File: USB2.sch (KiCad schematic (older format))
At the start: 26 parts

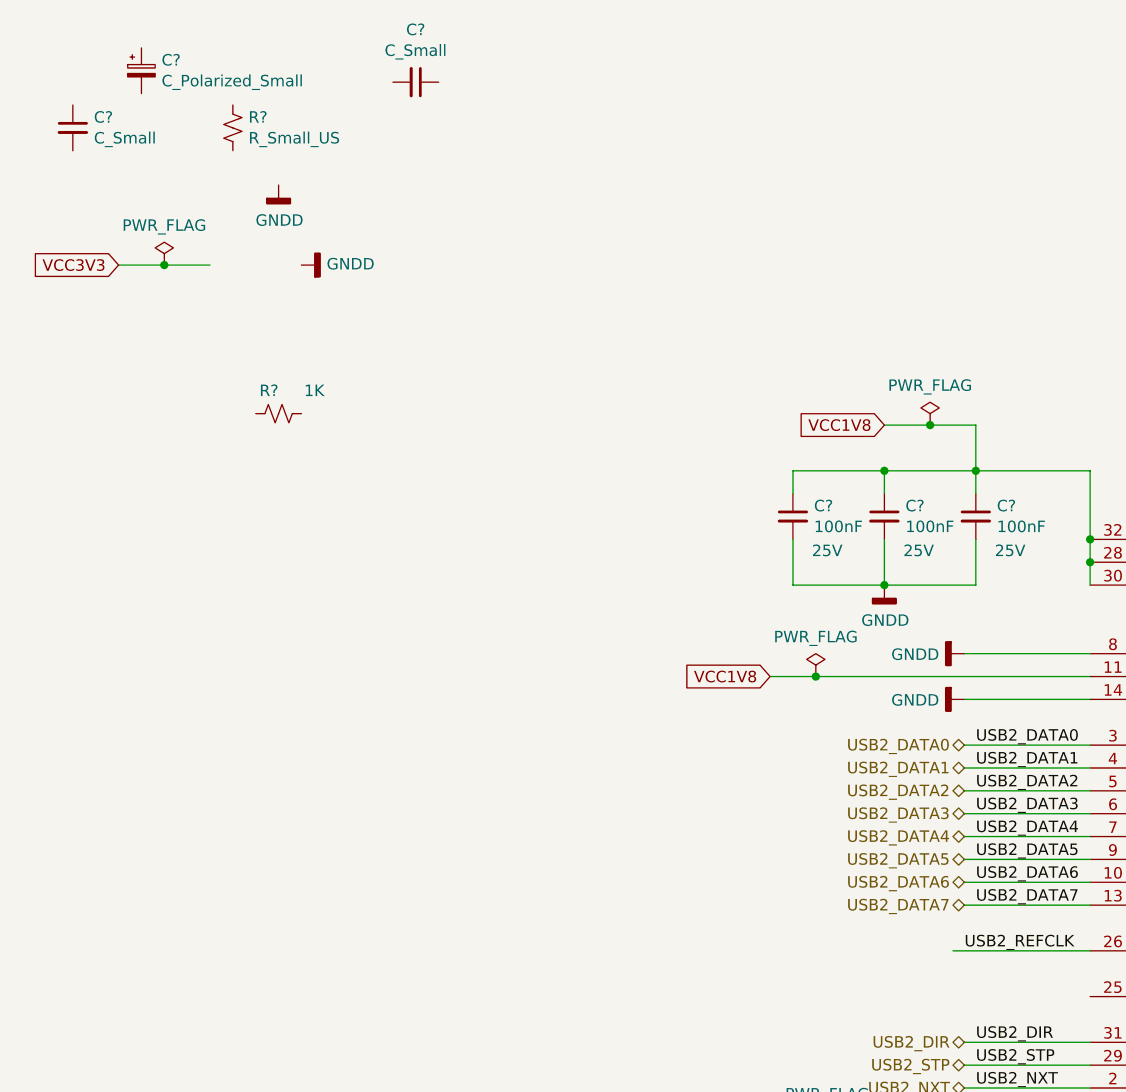
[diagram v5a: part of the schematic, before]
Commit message: Added bus lines -ETH_PHY_CONN -RAM -USB2 Made Output the port direction of clkout of Clock_Gen Placed sheet entris of sheet symbols on top sheet
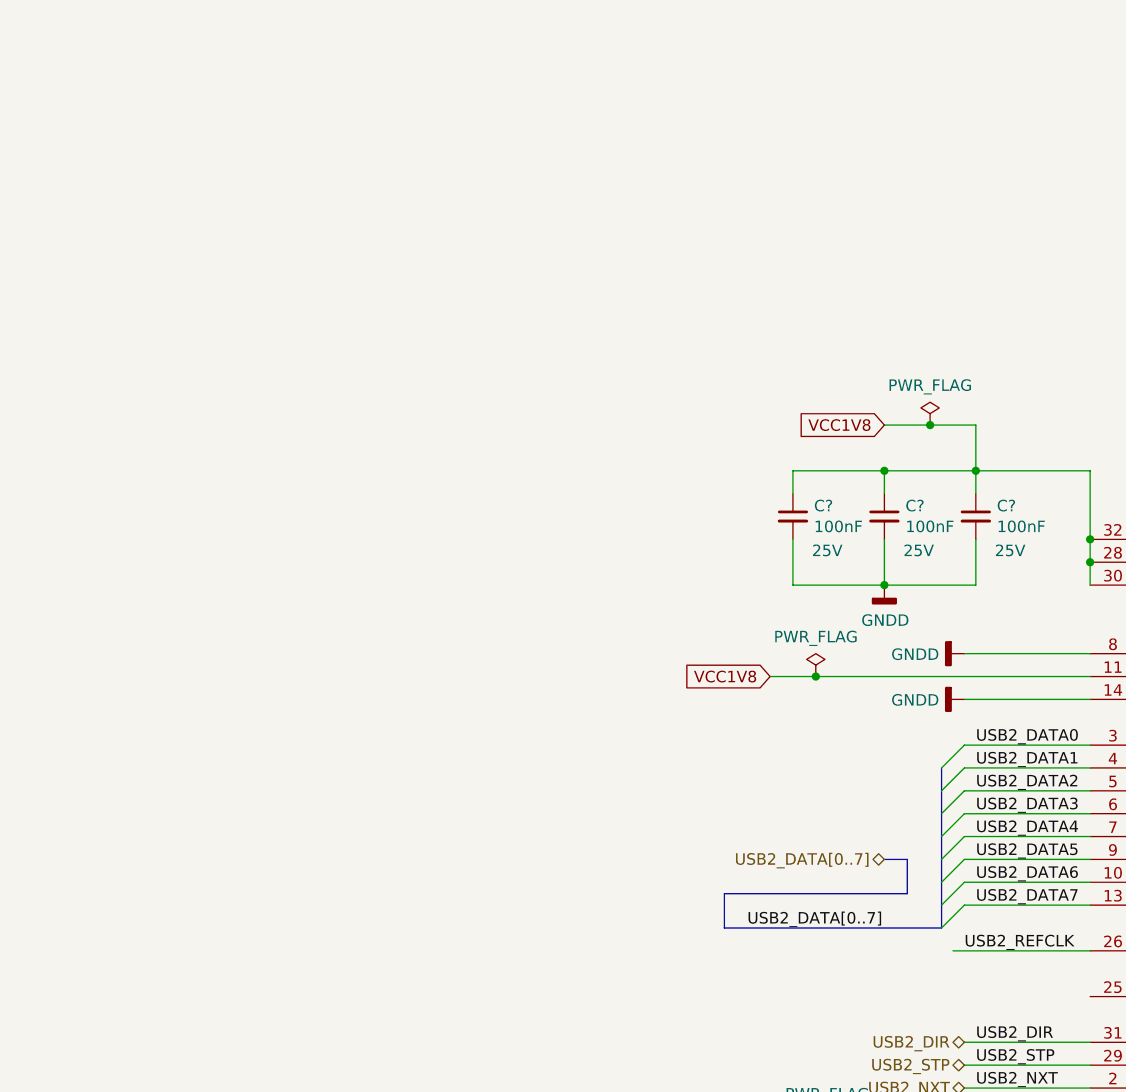
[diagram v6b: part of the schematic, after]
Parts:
- removed C?: C_Small, Capacitor_SMD:C_0603_1608Metric_Pad1.08x0.95mm_HandSolder, symbol Device:C_Small
- removed C?: C_Polarized_Small, Capacitor_Tantalum_SMD:CP_EIA-1608-10_AVX-L_Pad1.25x1.05mm_HandSolder, symbol Device:C_Polarized_Small
- removed C?: C_Small, symbol Device:C_Small
- removed R?: R_Small_US, Resistor_SMD:R_0603_1608Metric_Pad0.98x0.95mm_HandSolder, symbol Device:R_Small_US
- removed R?: 1K, Resistor_SMD:R_0603_1608Metric_Pad0.98x0.95mm_HandSolder, symbol Device:R_Small_US
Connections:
- net labels added: USB2_DATA[0..7]
- wire segments 113 -> 111
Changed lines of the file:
@@
 $Descr A4 11693 8268
 encoding utf-8
-Sheet 7 19
+Sheet 7 20
 Title "CGMPCX1006"
 Date "2021-02-03"
@@
 	-1   0    0    -1
 $EndComp
-$Comp
-L Device:R_Small_US R?
-U 1 1 602EE6FB
-P -1100 700
-AR Path="/601E7C5A/602EE6FB" Ref="R?"  Part="1"
-AR Path="/601E7CC8/602EE6FB" Ref="R?"  Part="1"
-AR Path="/601E7C92/602EE6FB" Ref="R?"  Part="1"
-AR Path="/601E7C92/60257FE5/602EE6FB" Ref="R?"  Part="1"
-AR Path="/601E7B38/602EE6FB" Ref="R?"  Part="1"
-AR Path="/601E7BF0/602EE6FB" Ref="R?"  Part="1"
-F 0 "R?" H -1032 746 50  0000 L CNN
-F 1 "R_Small_US" H -1032 655 50  0000 L CNN
-F 2 "Resistor_SMD:R_0603_1608Metric_Pad0.98x0.95mm_HandSolder" H -1100 700 50  0001 C CNN
-F 3 "~" H -1100 700 50  0001 C CNN
-	1    -1100 700
-	1    0    0    -1
-$EndComp
-$Comp
-L Device:C_Small C?
-U 1 1 602EE702
-P -1800 700
-AR Path="/601E7C5A/602EE702" Ref="C?"  Part="1"
-AR Path="/601E7CC8/602EE702" Ref="C?"  Part="1"
-AR Path="/601E7C92/602EE702" Ref="C?"  Part="1"
-AR Path="/601E7C92/60257FE5/602EE702" Ref="C?"  Part="1"
-AR Path="/601E7B38/602EE702" Ref="C?"  Part="1"
-AR Path="/601E7BF0/602EE702" Ref="C?"  Part="1"
-F 0 "C?" H -1708 746 50  0000 L CNN
-F 1 "C_Small" H -1708 655 50  0000 L CNN
-F 2 "Capacitor_SMD:C_0603_1608Metric_Pad1.08x0.95mm_HandSolder" H -1800 700 50  0001 C CNN
-F 3 "~" H -1800 700 50  0001 C CNN
-F 4 "" H -1800 700 50  0000 C CNN "Voltage"
-	1    -1800 700
-	1    0    0    -1
-$EndComp
-Text GLabel -1600 1300 0    50   Input ~ 0
-VCC3V3
-$Comp
-L power:PWR_FLAG #FLG?
-U 1 1 602EE709
-P -1400 1300
-AR Path="/601E7C5A/602EE709" Ref="#FLG?"  Part="1"
-AR Path="/601E7CC8/602EE709" Ref="#FLG?"  Part="1"
-AR Path="/601E7C92/602EE709" Ref="#FLG?"  Part="1"
-AR Path="/601E7C92/60257FE5/602EE709" Ref="#FLG?"  Part="1"
-AR Path="/601E7B38/602EE709" Ref="#FLG?"  Part="1"
-AR Path="/601E7BF0/602EE709" Ref="#FLG?"  Part="1"
-F 0 "#FLG?" H -1400 1375 50  0001 C CNN
-F 1 "PWR_FLAG" H -1400 1473 50  0000 C CNN
-F 2 "" H -1400 1300 50  0001 C CNN
-F 3 "~" H -1400 1300 50  0001 C CNN
-	1    -1400 1300
-	1    0    0    -1
-$EndComp
-Connection ~ -1400 1300
-Wire Wire Line
-	-1400 1300 -1200 1300
-Wire Wire Line
-	-1600 1300 -1400 1300
-$Comp
-L power:GNDD #PWR?
-U 1 1 602EE712
-P -900 950
-AR Path="/601DF0A6/602EE712" Ref="#PWR?"  Part="1"
-AR Path="/601E7C5A/602EE712" Ref="#PWR?"  Part="1"
-AR Path="/601E7CC8/602EE712" Ref="#PWR?"  Part="1"
-AR Path="/601E7C92/602EE712" Ref="#PWR?"  Part="1"
-AR Path="/601E7C92/60257FE5/602EE712" Ref="#PWR?"  Part="1"
-AR Path="/601E7B38/602EE712" Ref="#PWR?"  Part="1"
-AR Path="/601E7BF0/602EE712" Ref="#PWR?"  Part="1"
-F 0 "#PWR?" H -900 700 50  0001 C CNN
-F 1 "GNDD" H -896 795 50  0000 C CNN
-F 2 "" H -900 950 50  0001 C CNN
-F 3 "" H -900 950 50  0001 C CNN
-	1    -900 950
-	1    0    0    -1
-$EndComp
-$Comp
-L Device:C_Polarized_Small C?
-U 1 1 602EE719
-P -1500 450
-AR Path="/601E7C92/602EE719" Ref="C?"  Part="1"
-AR Path="/601E7C92/60257FE5/602EE719" Ref="C?"  Part="1"
-AR Path="/601E7B38/602EE719" Ref="C?"  Part="1"
-AR Path="/601E7BF0/602EE719" Ref="C?"  Part="1"
-F 0 "C?" H -1412 496 50  0000 L CNN
-F 1 "C_Polarized_Small" H -1412 405 50  0000 L CNN
-F 2 "Capacitor_Tantalum_SMD:CP_EIA-1608-10_AVX-L_Pad1.25x1.05mm_HandSolder" H -1500 450 50  0001 C CNN
-F 3 "~" H -1500 450 50  0001 C CNN
-F 4 "" H -1500 450 50  0000 C CNN "Voltage"
-	1    -1500 450
-	1    0    0    -1
-$EndComp
-$Comp
-L Device:C_Small C?
-U 1 1 602EE71F
-P -300 500
-F 0 "C?" V -529 500 50  0000 C CNN
-F 1 "C_Small" V -438 500 50  0000 C CNN
-F 2 "" H -300 500 50  0001 C CNN
-F 3 "~" H -300 500 50  0001 C CNN
-	1    -300 500
-	0    1    1    0
-$EndComp
 Text GLabel 1750 2000 0    50   Input ~ 0
 VCC1V8
@@
 $Comp
 L power:GNDD #PWR?
-U 1 1 602DFDE2
-P -800 1300
-F 0 "#PWR?" H -800 1050 50  0001 C CNN
-F 1 "GNDD" V -796 1190 50  0000 R CNN
-F 2 "" H -800 1300 50  0001 C CNN
-F 3 "" H -800 1300 50  0001 C CNN
-	1    -800 1300
-	0    -1   -1   0
-$EndComp
-$Comp
-L power:GNDD #PWR?
 U 1 1 602E0977
 P 2100 3000
@@
 	0    1    1    0
 $EndComp
-Text HLabel 2100 3400 0    50   BiDi ~ 0
-USB2_DATA0
-Text HLabel 2100 3500 0    50   BiDi ~ 0
-USB2_DATA1
-Text HLabel 2100 3600 0    50   BiDi ~ 0
-USB2_DATA2
-Text HLabel 2100 3700 0    50   BiDi ~ 0
-USB2_DATA3
-Text HLabel 2100 3800 0    50   BiDi ~ 0
-USB2_DATA4
-Text HLabel 2100 3900 0    50   BiDi ~ 0
-USB2_DATA5
-Text HLabel 2100 4000 0    50   BiDi ~ 0
-USB2_DATA6
-Text HLabel 2100 4100 0    50   BiDi ~ 0
-USB2_DATA7
+Text HLabel 1750 3900 0    50   BiDi ~ 0
+USB2_DATA[0..7]
 Text HLabel 2100 4700 0    50   BiDi ~ 0
 USB2_DIR
@@
 $Comp
 L Device:R_Small_US R?
-U 1 1 6031C16F
-P -900 1950
-AR Path="/601E7C5A/6031C16F" Ref="R?"  Part="1"
-AR Path="/601E7CC8/6031C16F" Ref="R?"  Part="1"
-AR Path="/601E7C92/6031C16F" Ref="R?"  Part="1"
-AR Path="/601E7C92/60257FE5/6031C16F" Ref="R?"  Part="1"
-AR Path="/601E7B38/6031C16F" Ref="R?"  Part="1"
-AR Path="/601E7BF0/6031C16F" Ref="R?"  Part="1"
-F 0 "R?" V -800 1950 50  0000 L CNN
-F 1 "1K" V -800 1750 50  0000 L CNN
-F 2 "Resistor_SMD:R_0603_1608Metric_Pad0.98x0.95mm_HandSolder" H -900 1950 50  0001 C CNN
-F 3 "~" H -900 1950 50  0001 C CNN
-	1    -900 1950
-	0    -1   -1   0
-$EndComp
-$Comp
-L Device:R_Small_US R?
 U 1 1 6031CE7F
 P 4150 3650
@@
 Wire Wire Line
 	9100 3300 9200 3300
+Entry Wire Line
+	2000 3500 2100 3400
+Entry Wire Line
+	2000 3600 2100 3500
+Entry Wire Line
+	2000 3700 2100 3600
+Entry Wire Line
+	2000 3800 2100 3700
+Entry Wire Line
+	2000 3900 2100 3800
+Entry Wire Line
+	2000 4000 2100 3900
+Entry Wire Line
+	2000 4100 2100 4000
+Entry Wire Line
+	2000 4200 2100 4100
+Wire Bus Line
+	2000 4200 1050 4200
+Wire Bus Line
+	1050 4050 1850 4050
+Wire Bus Line
+	1850 3900 1750 3900
+Wire Bus Line
+	1850 3900 1850 4050
+Wire Bus Line
+	1050 4050 1050 4200
+Text Label 1150 4200 0    50   ~ 0
+USB2_DATA[0..7]
+Wire Bus Line
+	2000 3500 2000 4200
 $EndSCHEMATC
